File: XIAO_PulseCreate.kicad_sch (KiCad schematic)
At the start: 14 parts, among them J1 MA735, J2 I2C OLED 0.91', J3 Power/Solenoid, J4 Trigger_IN, J5 Trigger_Out, Q1 2SK2232, SW1 MODE, SW2 +, SW3 -, U1 XIAO-RP2040-DIP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

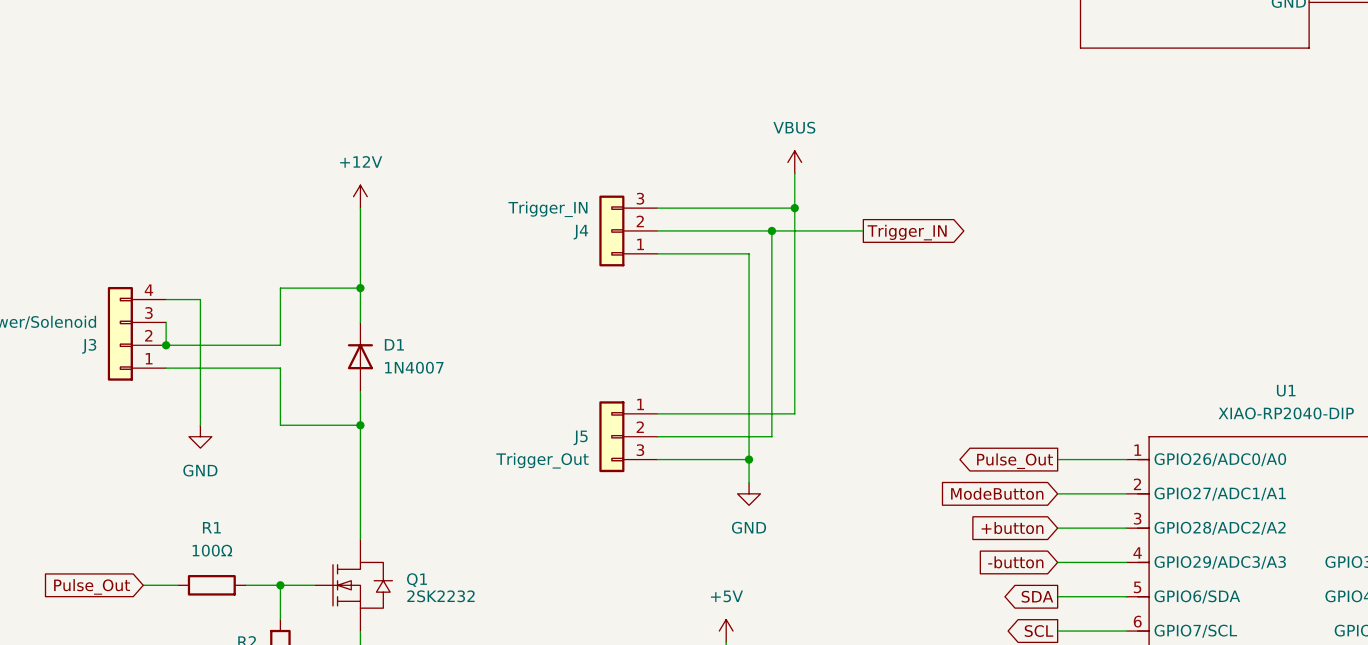
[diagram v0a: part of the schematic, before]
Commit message: Trigger_INの分圧抵抗を追加。 基板のソレノイドと電源の表記が逆だったので修正
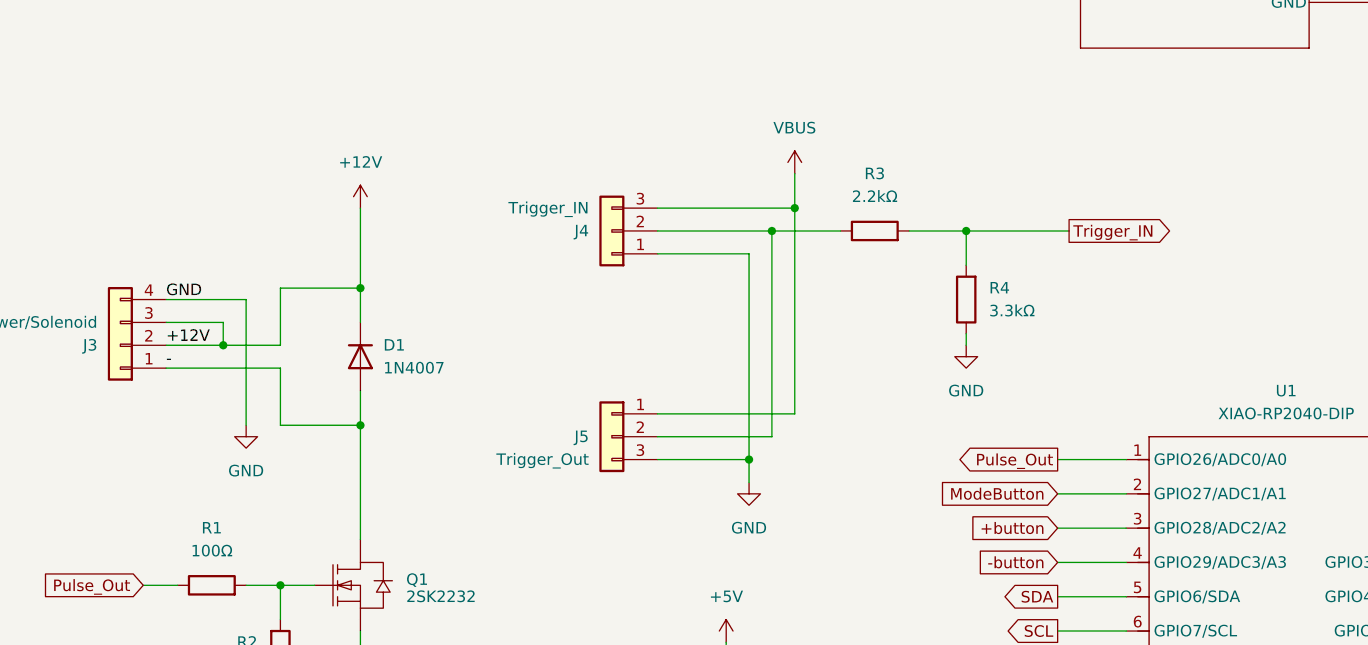
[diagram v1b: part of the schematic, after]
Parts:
- added R3: 2.2kΩ, Resistor_THT:R_Axial_DIN0207_L6.3mm_D2.5mm_P10.16mm_Horizontal, symbol Device:R
- added R4: 3.3kΩ, Resistor_THT:R_Axial_DIN0207_L6.3mm_D2.5mm_P10.16mm_Horizontal, symbol Device:R
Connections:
- net GND: now also R4.1
- net Trigger_IN: now also R3.2, R4.2; no longer J4.2 (Pin_2), J5.2 (Pin_2)
- net -: now reaches D1.2 (A), J3.1 (Pin_1), Q1.2 (D)
- new net: J4.2 (Pin_2), J5.2 (Pin_2), R3.1

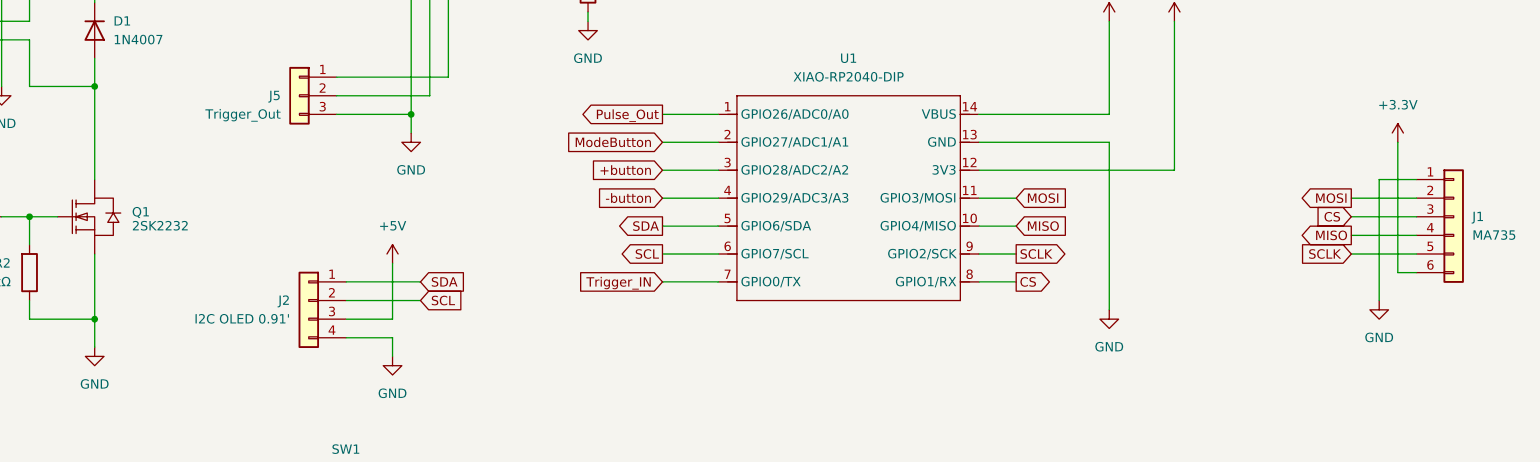
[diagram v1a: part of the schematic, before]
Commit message: MOSFETをIRLZ34Nに変更
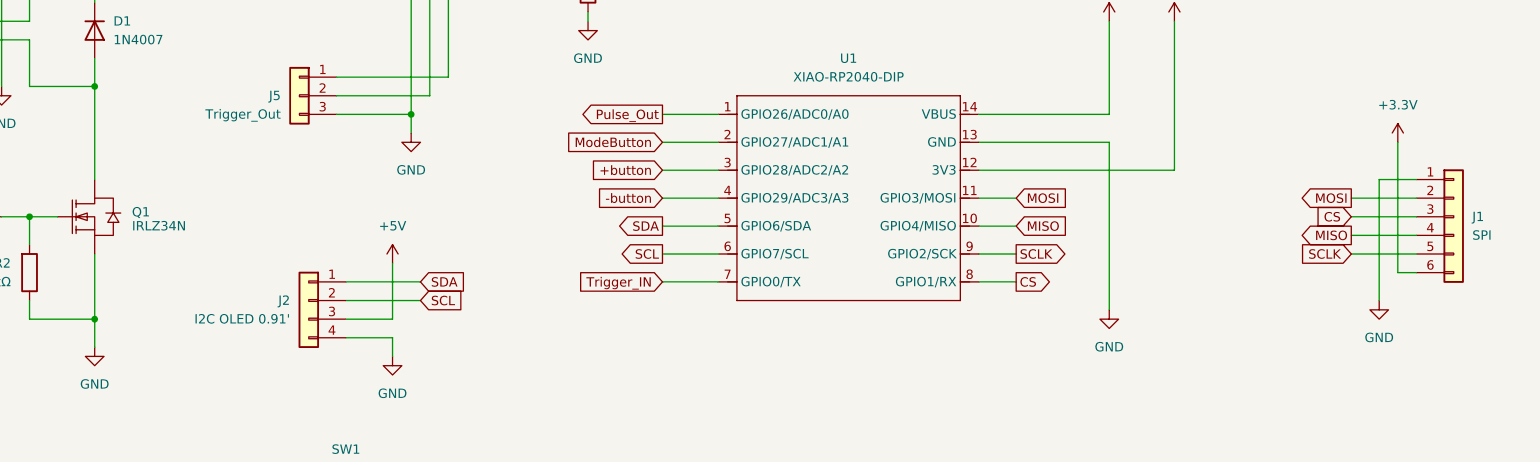
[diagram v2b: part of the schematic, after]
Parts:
- J1: value MA735 -> SPI
- Q1: value 2SK2232 -> IRLZ34N
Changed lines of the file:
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@@
 	(title_block
 		(title "XIAO PluseCreate PCB")
-		(date "2025-02-11")
-		(rev "1.02")
+		(date "2025-02-19")
+		(rev "1.03")
 		(company "Chibi-T International")
 		(comment 1 "Tomohiro Kusu")
@@
 			)
 		)
-		(property "Value" "2SK2232"
+		(property "Value" "IRLZ34N"
 			(at 68.58 107.95 0)
 			(effects
@@
 			)
 		)
-		(property "Value" "MA735"
+		(property "Value" "SPI"
 			(at 251.46 109.2199 0)
 			(effects
